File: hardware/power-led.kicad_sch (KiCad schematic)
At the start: 13 parts, among them J3 5V INPUT, J7 RING 5V, Q1 AO3401A, U1 SN74AHCT1G125

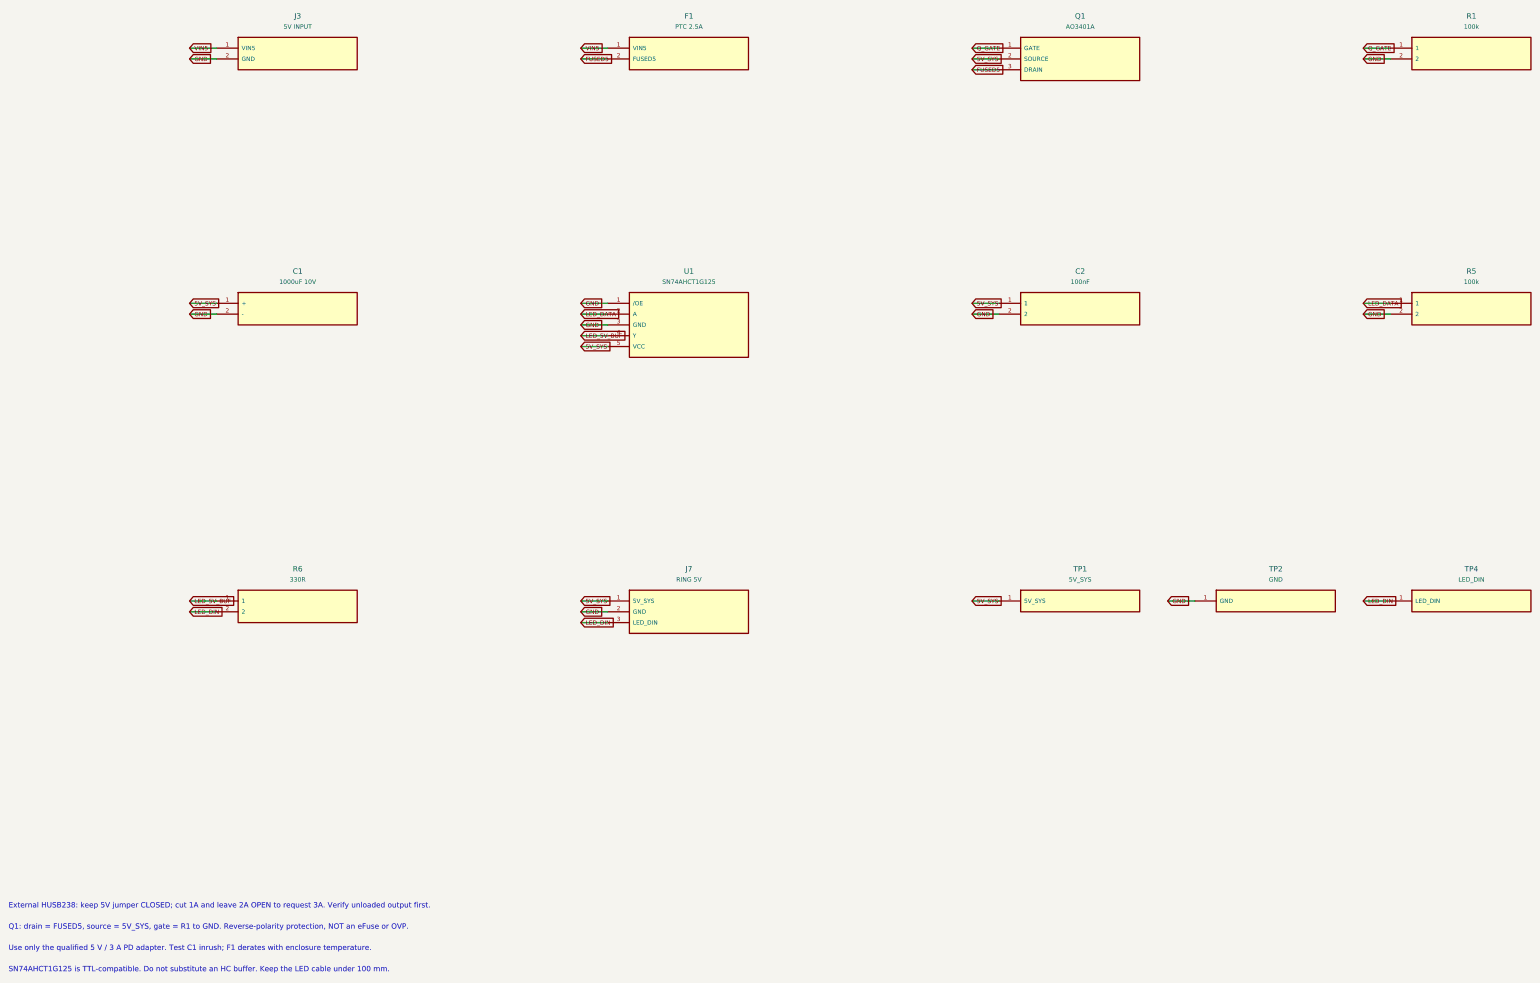
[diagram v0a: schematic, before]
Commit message: engineering: Rev B zero-interference CAD, sealed STL meshes and carrier corrections
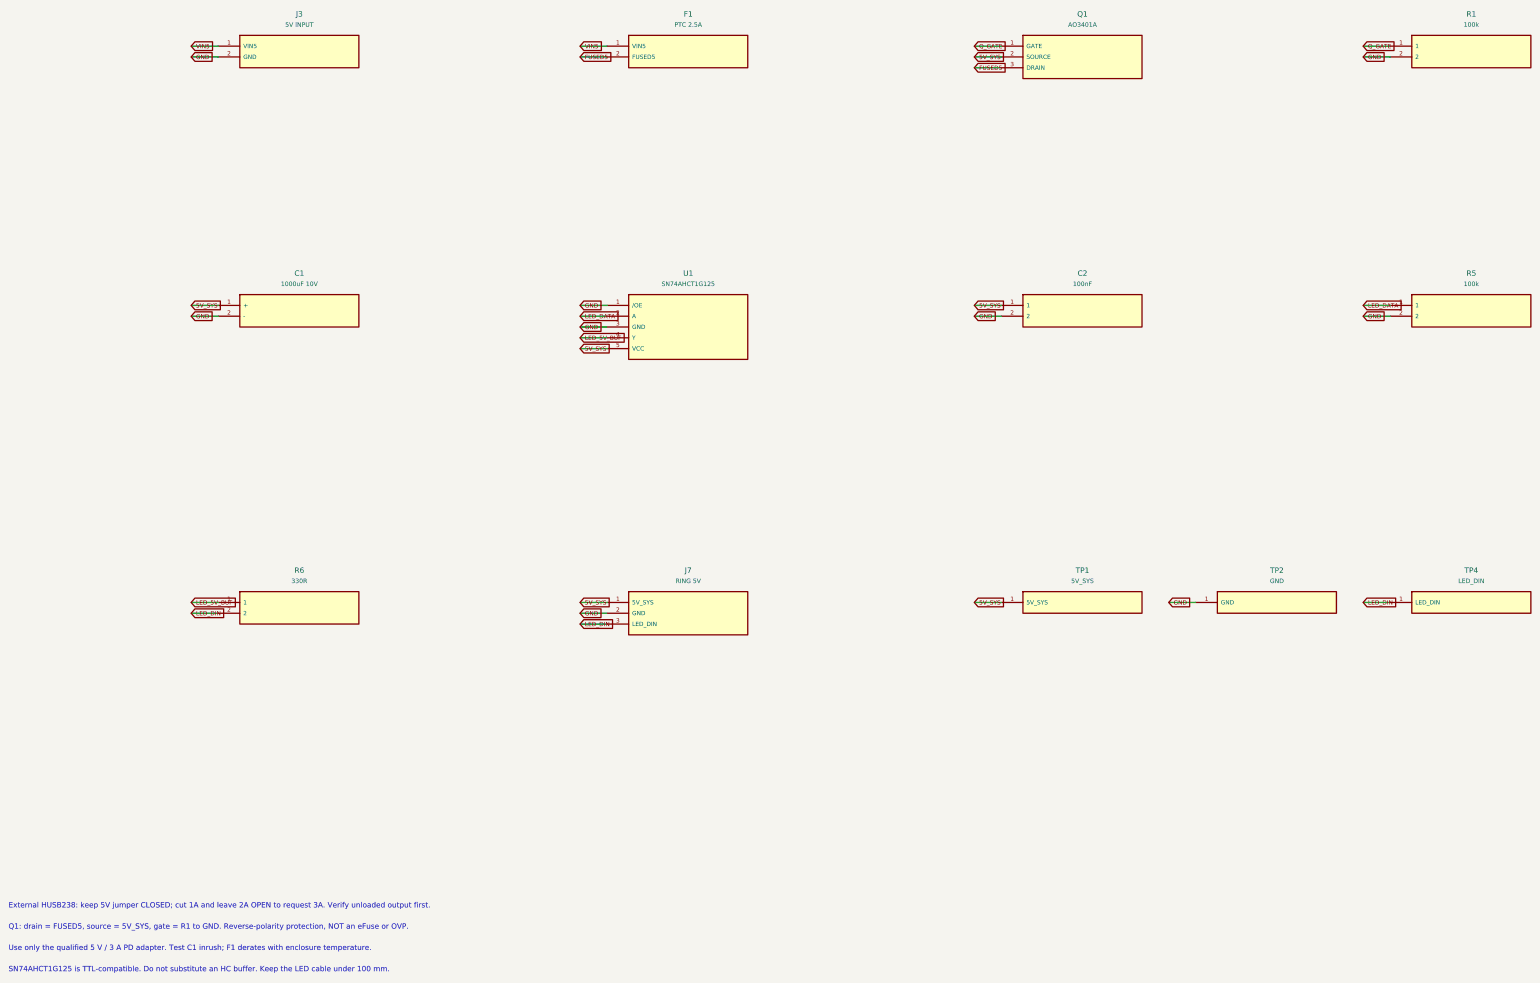
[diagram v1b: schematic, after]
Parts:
- C1: footprint Aether:CP_Radial_D10_P5 -> Aether:CP_Radial_D10_P5_C1
- C2: footprint Aether:C_0805_2012Metric -> Aether:C_0805_2012Metric_C2
- F1: footprint Aether:PTC_P5.08 -> Aether:PTC_P5.08_F1
- J3: footprint Aether:Terminal_1x02_P5.08 -> Aether:Terminal_1x02_P5.08_J3
- J7: footprint Aether:XH_1x03_P2.50 -> Aether:XH_1x03_P2.50_J7
- Q1: footprint Aether:SOT-23 -> Aether:SOT-23_Q1
- R1: footprint Aether:R_0805_2012Metric -> Aether:R_0805_2012Metric_R1
- R5: footprint Aether:R_0805_2012Metric -> Aether:R_0805_2012Metric_R5
- R6: footprint Aether:R_0805_2012Metric -> Aether:R_0805_2012Metric_R6
- TP1: footprint Aether:TestPoint_THT_D2 -> Aether:TestPoint_THT_D2_TP1
- TP2: footprint Aether:TestPoint_THT_D2 -> Aether:TestPoint_THT_D2_TP2
- TP4: footprint Aether:TestPoint_THT_D2 -> Aether:TestPoint_THT_D2_TP4
- U1: footprint Aether:SOT-23-5 -> Aether:SOT-23-5_U1
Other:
- moved on the sheet: C1, C2, J3, Q1, R6, TP1, U1
